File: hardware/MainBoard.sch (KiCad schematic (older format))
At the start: 47 parts, among them J10 B2_HDR_LEFT, J11 B2_HDR_RIGHT, J9 POWER, Q1 2N3904, Q2 2N3904, Q3 2N3904, U1 ATtiny85, U2 TL074, U3 78L05, U4 79L05

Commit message: [JNTUB-HW] JNTUB Hardware Revision 0.2
* Add resistor to drain C12 (PWM filter cap)
* Add optional parallel resistor to PWM filter
  * selectable by jumper
  * increases the cutoff frequency to audio range
* Add resistor between 5V and MCU RESET to allow for ISP
* Move a few resistors to Board 1
* Add ISP programming headers!
* Change all resistors and diodes to standing
* Shorten pin headers that connect Boards 1 and 2
* Ditch ground pour on Board 1 in favor of direct traces
* Move CV 1 and CV 2 jacks down a bit
* Slightly adjust LED positions
* Adjust front panel to match moved components
* Tweak design of front panel
* Fix up some 3D models
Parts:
- removed R17: 330k, SDIY:R_Axial_DIN0204_L3.6mm_D1.6mm_P5.08mm_Horizontal, symbol Device:R
- removed R21: R_out, SDIY:R_Axial_DIN0204_L3.6mm_D1.6mm_P5.08mm_Horizontal, symbol Device:R
- added J12: ISP, Pin_Headers:Pin_Header_Straight_2x03_Pitch2.54mm, symbol Connector:AVR-ISP-6
- added JP2: JMP_AUDIO, Pin_Headers:Pin_Header_Straight_1x02_Pitch2.54mm, symbol Device:Jumper_NO_Small
- added R26: 10k, Resistors_THT:R_Axial_DIN0207_L6.3mm_D2.5mm_P2.54mm_Vertical, symbol Device:R
- added R27: R_filb, Resistors_THT:R_Axial_DIN0207_L6.3mm_D2.5mm_P2.54mm_Vertical, symbol Device:R
- added R28: 100k, Resistors_THT:R_Axial_DIN0207_L6.3mm_D2.5mm_P2.54mm_Vertical, symbol Device:R
- C12: value C_filt -> C_fil
- D1, D3: footprint SDIY:D_DO-35_SOD27_P6.85mm_Horizontal -> Diodes_THT:D_DO-35_SOD27_P2.54mm_Vertical_AnodeUp
- D2, D4, D5: footprint SDIY:D_DO-35_SOD27_P6.85mm_Horizontal -> Diodes_THT:D_DO-35_SOD27_P2.54mm_Vertical_KathodeUp
- J10, J11: footprint Pin_Headers:Pin_Header_Straight_1x09_Pitch2.54mm -> Pin_Headers:Pin_Header_Straight_1x07_Pitch2.54mm; symbol Connector:Conn_01x09_Female -> Connector:Conn_01x07_Female
- JP1: value JMP_GATE_OUT -> JMP_UNIPOLAR
- R10, R11, R12, R13, R14, R16, R18, R19, R2, R20, R23, R24, R25, R4, R5, R6, R8: footprint SDIY:R_Axial_DIN0204_L3.6mm_D1.6mm_P5.08mm_Horizontal -> Resistors_THT:R_Axial_DIN0207_L6.3mm_D2.5mm_P2.54mm_Vertical
- R22: value R_filt -> R_fila; footprint SDIY:R_Axial_DIN0204_L3.6mm_D1.6mm_P5.08mm_Horizontal -> Resistors_THT:R_Axial_DIN0207_L6.3mm_D2.5mm_P2.54mm_Vertical
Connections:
- net +5V: now also R14.1, R19.1, J12.2 (VCC), R26.1; no longer R14.2, R19.2, U1.1 (~RESET~/PB5)
- net -12V: now also U4.2 (VI); no longer U4.3 (VO)
- net -5V: now also U4.3 (VO); no longer U4.2 (VI)
- net CLK_TRG: now also J11.6 (Pin_6); no longer J11.8 (Pin_8)
- net GNDREF: now also R11.1, R5.1, J12.6 (GND), R28.2; no longer J10.3 (Pin_3), J10.4 (Pin_4), J10.5 (Pin_5), J11.5 (Pin_5), J11.6 (Pin_6), R11.2, R5.2
- net MCU_ADC1: now also D1.2 (A), D2.1 (K), R2.2, R4.2, J12.3 (SCK); no longer D3.2 (A), D4.1 (K), R10.2, R8.2
- net MCU_ADC2: now also D3.2 (A), D4.1 (K), R10.2, R8.2; no longer D1.2 (A), D2.1 (K), R2.2, R4.2
- net MCU_ADC3: now also J10.6 (Pin_6); no longer J10.8 (Pin_8)
- net MCU_PB0: now also R14.2, J12.4 (MOSI); no longer R14.1
- net MCU_PWM: now also J12.1 (MISO), JP2.2, R28.1
- net OUT: now also JP1.2, R23.2, R25.2, U2.14
- net P1_AVG: now also J11.7 (Pin_7), U2.10 (+); no longer J10.9 (Pin_9), U2.5 (+)
- net P2_AVG: now also J10.7 (Pin_7), U2.5 (+); no longer J11.9 (Pin_9), U2.10 (+)
- net at R10.1, R12.1: now also U2.7; no longer U2.8
- net at Q3.3 (C): now also R19.2; no longer R19.1
- net at C12.1, R22.2, U2.12 (+): now also R27.2
- net IN_LED+ renamed CLK_LED
- net CLK_LED: now also J11.5 (Pin_5); no longer J11.7 (Pin_7)
- removed net OUT_LED+: J10.7 (Pin_7), R23.2, U2.2 (-)
- net OUT_LED- renamed LED_NEG
- net LED_NEG: now also J10.4 (Pin_4); no longer J10.6 (Pin_6)
- new net: R5.2, R6.1, U2.9 (-)
- new net: R4.1, R6.2, U2.8
- new net: R11.2, R12.2, U2.6 (-)
- new net: JP2.1, R27.1
- new net LED_POS: J10.5 (Pin_5), R23.1, U2.2 (-)
- new net MCU_RESET: J12.5 (~RST), R26.2, U1.1 (~RESET~/PB5)
- no-connect marks 0 -> 1
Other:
- note added: "330k"
- note added: "NOTES:\n\n- R_led: Will depend on the color & desired brightness. I use 5.6k for my red LEDs.\n\n- R_fila/R_filb/C_filt: Set for desired PWM filter frequencies.\n I use: R_fila = 68k R_filb = 8.2k C_filt = 2.2n\n With these values, the cutoff frequencies are:\n 1 kHz (JMP_AUDIO not set)\n 9.9 kHz (JMP_AUDIO set)\n\n- 10k resistors throughout can be replaced with anything 10k-100k.\n\n- Regular sw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"
- note added: "PWM filter"
- note added: "R17 (on Board 1)"
- note removed: "NOTES:\n\n- R_out: Use 1k for 1/4W resistors. Use 2k for 1/8W resistors.\n\n- R_led: Will depend on the color & desired brightness. I use 5.6k for my red LEDs.\n\n- R_filt/C_filt: Set for desired PWM filter freq*.\n For ATtiny85’s max 250kHz PWM, 5kHz cutoff serves well, giving:\n R_filt=47k C_filt=680p\n\n- 10k resistors in PARAM 1 and PARAM 2 can be replaced with anything 10k-100k.\n\n- Schottk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"
- moved on the sheet: C10, C12, D5, JP1, Q1, Q2, Q3, R13, R14, R16, R18, R19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

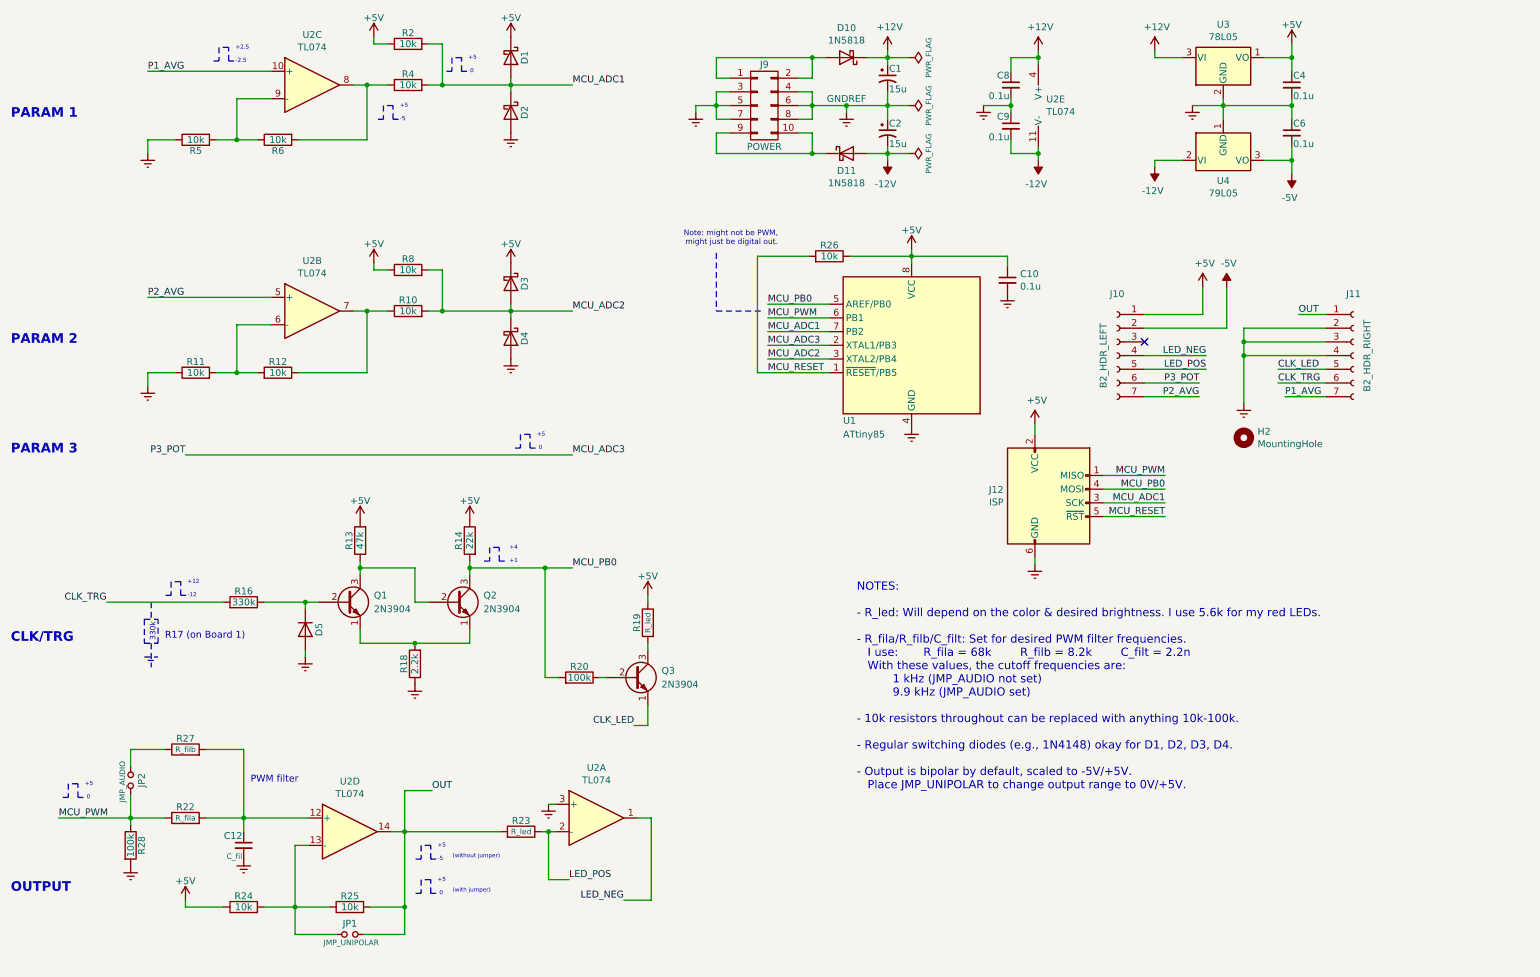
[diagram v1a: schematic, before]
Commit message: [JNTUB-HW] Modify resistor values in schematic
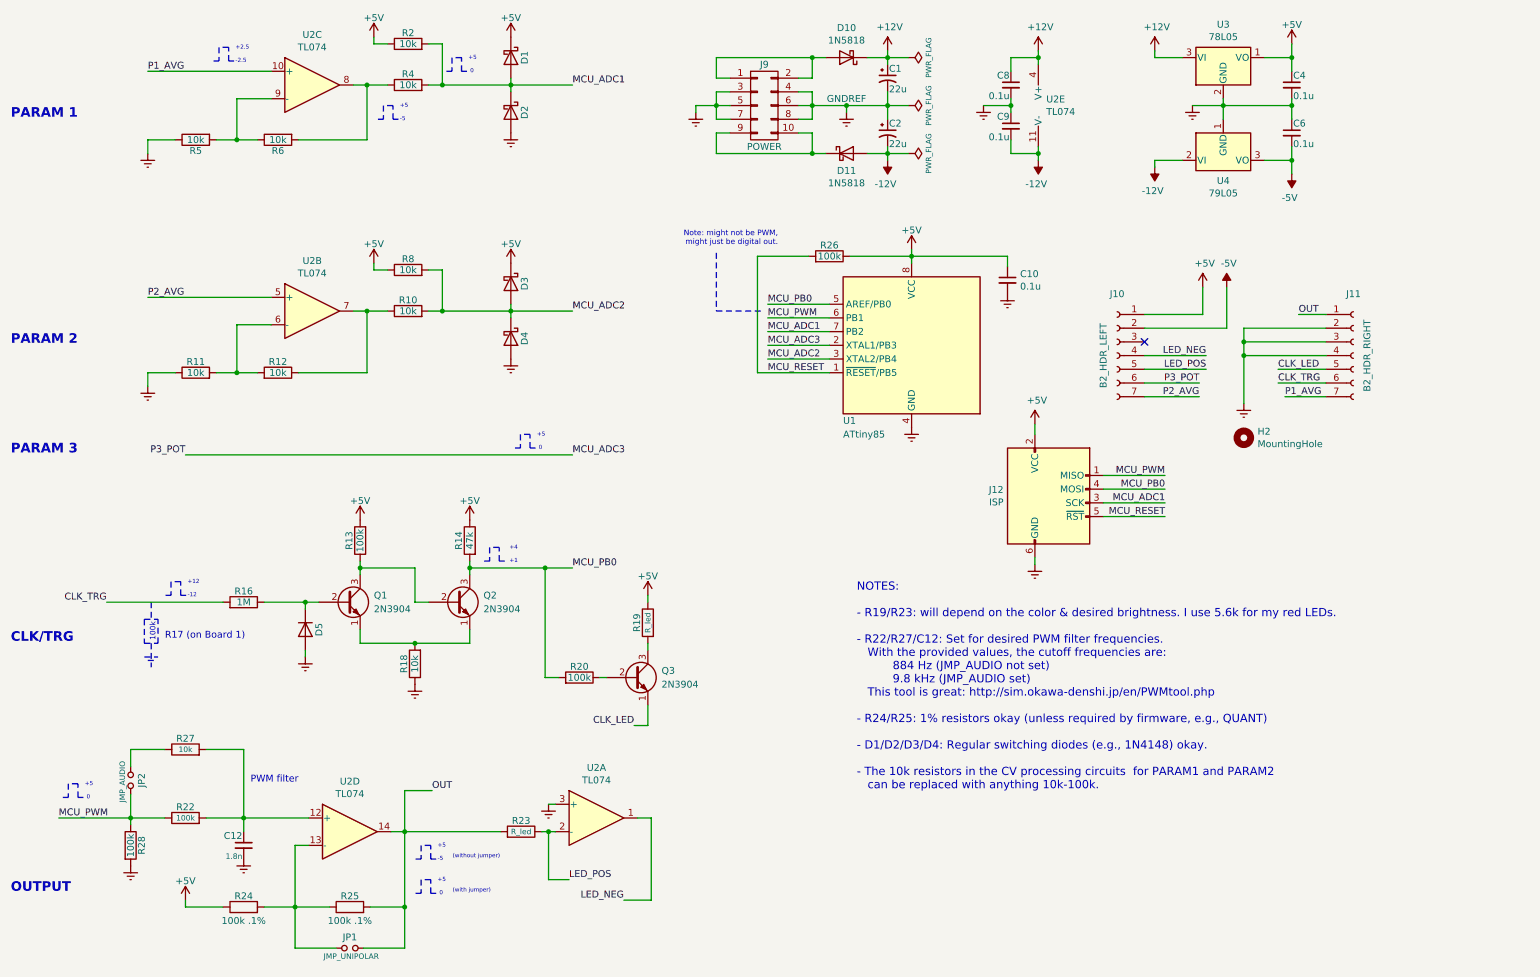
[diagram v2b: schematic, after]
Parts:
- C1, C2: value 15u -> 22u
- C12: value C_fil -> 1.8n
- R13: value 47k -> 100k
- R14: value 22k -> 47k
- R16: value 330k -> 1M
- R18: value 2.2k -> 10k
- R22: value R_fila -> 100k
- R24, R25: value 10k -> 100k .1%
- R26: value 10k -> 100k
- R27: value R_filb -> 10k
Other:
- note added: "100k"
- note added: "NOTES:\n\n- R19/R23: will depend on the color & desired brightness. I use 5.6k for my red LEDs.\n\n- R22/R27/C12: Set for desired PWM filter frequencies.\n With the provided values, the cutoff frequencies are:\n 884 Hz (JMP_AUDIO not set)\n 9.8 kHz (JMP_AUDIO set)\n This tool is great: http://sim.okawa-denshi.jp/en/PWMtool.php\n\n- R24/R25: 1% resistors okay (unless required by firmware, e.g., QU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"
- note removed: "330k"
- note removed: "NOTES:\n\n- R_led: Will depend on the color & desired brightness. I use 5.6k for my red LEDs.\n\n- R_fila/R_filb/C_filt: Set for desired PWM filter frequencies.\n I use: R_fila = 68k R_filb = 8.2k C_filt = 2.2n\n With these values, the cutoff frequencies are:\n 1 kHz (JMP_AUDIO not set)\n 9.9 kHz (JMP_AUDIO set)\n\n- 10k resistors throughout can be replaced with anything 10k-100k.\n\n- Regular sw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"
- moved on the sheet: JP1
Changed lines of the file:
@@
 P 2500 5025
 F 0 "R16" V 2580 5025 50  0000 C CNN
-F 1 "330k" V 2500 5025 50  0000 C CNN
+F 1 "1M" V 2500 5025 50  0000 C CNN
 F 2 "Resistors_THT:R_Axial_DIN0207_L6.3mm_D2.5mm_P2.54mm_Vertical" V 2430 5025 50  0001 C CNN
 F 3 "" H 2500 5025 50  0001 C CNN
@@
 P 3350 4575
 F 0 "R13" V 3430 4575 50  0000 C CNN
-F 1 "47k" V 3350 4575 50  0000 C CNN
+F 1 "100k" V 3350 4575 50  0000 C CNN
 F 2 "Resistors_THT:R_Axial_DIN0207_L6.3mm_D2.5mm_P2.54mm_Vertical" V 3280 4575 50  0001 C CNN
 F 3 "" H 3350 4575 50  0001 C CNN
@@
 P 3275 7250
 F 0 "R25" V 3355 7250 50  0000 C CNN
-F 1 "10k" V 3275 7250 50  0000 C CNN
+F 1 "100k .1%" V 3175 7250 50  0000 C CNN
 F 2 "Resistors_THT:R_Axial_DIN0207_L6.3mm_D2.5mm_P2.54mm_Vertical" V 3205 7250 50  0001 C CNN
 F 3 "" H 3275 7250 50  0001 C CNN
@@
 P 2500 7250
 F 0 "R24" V 2580 7250 50  0000 C CNN
-F 1 "10k" V 2500 7250 50  0000 C CNN
+F 1 "100k .1%" V 2400 7250 50  0000 C CNN
 F 2 "Resistors_THT:R_Axial_DIN0207_L6.3mm_D2.5mm_P2.54mm_Vertical" V 2430 7250 50  0001 C CNN
 F 3 "" H 2500 7250 50  0001 C CNN
@@
 Connection ~ 2875 7250
 Wire Wire Line
-	2875 7450 3175 7450
+	2875 7550 3175 7550
 $Comp
 L Device:Jumper_NO_Small JP1
 U 1 1 5FEB5E16
-P 3275 7450
-F 0 "JP1" H 3275 7530 50  0000 C CNN
-F 1 "JMP_UNIPOLAR" H 3285 7390 40  0000 C CNN
-F 2 "Pin_Headers:Pin_Header_Straight_1x02_Pitch2.54mm" H 3275 7450 50  0001 C CNN
-F 3 "" H 3275 7450 50  0001 C CNN
-	1    3275 7450
-	1    0    0    -1
-$EndComp
-Wire Wire Line
-	3675 7450 3375 7450
+P 3275 7550
+F 0 "JP1" H 3275 7630 50  0000 C CNN
+F 1 "JMP_UNIPOLAR" H 3285 7490 40  0000 C CNN
+F 2 "Pin_Headers:Pin_Header_Straight_1x02_Pitch2.54mm" H 3275 7550 50  0001 C CNN
+F 3 "" H 3275 7550 50  0001 C CNN
+	1    3275 7550
+	1    0    0    -1
+$EndComp
+Wire Wire Line
+	3675 7550 3375 7550
 Connection ~ 3675 7250
 $Comp
@@
 P 2500 6800
 F 0 "C12" H 2510 6870 50  0000 L CNN
-F 1 "C_fil" H 2510 6720 40  0000 L CNN
+F 1 "1.8n" H 2510 6720 40  0000 L CNN
 F 2 "Capacitors_THT:C_Disc_D4.3mm_W1.9mm_P5.00mm" H 2500 6800 50  0001 C CNN
 F 3 "" H 2500 6800 50  0001 C CNN
@@
 P 2075 6600
 F 0 "R22" V 2155 6600 50  0000 C CNN
-F 1 "R_fila" V 2075 6600 40  0000 C CNN
+F 1 "100k" V 2075 6600 40  0000 C CNN
 F 2 "Resistors_THT:R_Axial_DIN0207_L6.3mm_D2.5mm_P2.54mm_Vertical" V 2005 6600 50  0001 C CNN
 F 3 "" H 2075 6600 50  0001 C CNN
@@
 	4700 4775 4700 5575
 Wire Wire Line
-	2875 7250 2875 7450
+	2875 7250 2875 7550
 Wire Wire Line
 	2875 7250 3125 7250
 Wire Wire Line
-	3675 7250 3675 7450
+	3675 7250 3675 7550
 Wire Wire Line
 	2500 6600 2975 6600
@@
 OUTPUT
 Text Notes 6975 6400 0    60   ~ 0
-NOTES:\n\n- R_led: Will depend on the color & desired brightness. I use 5.6k for my red LEDs.\n\n- R_fila/R_filb/C_filt: Set for desired PWM filter frequencies.\n   I use:       R_fila = 68k        R_filb = 8.2k        C_filt = 2.2n\n   With these values, the cutoff frequencies are:\n          1 kHz (JMP_AUDIO not set)\n          9.9 kHz (JMP_AUDIO set)\n\n- 10k resistors throughout can be replaced with anything 10k-100k.\n\n- Regular switching diodes (e.g., 1N4148) okay for D1, D2, D3, D4.\n\n- Output is bipolar by default, scaled to -5V/+5V.\n   Place JMP_UNIPOLAR to change output range to 0V/+5V.
+NOTES:\n\n- R19/R23: will depend on the color & desired brightness. I use 5.6k for my red LEDs.\n\n- R22/R27/C12: Set for desired PWM filter frequencies.\n   With the provided values, the cutoff frequencies are:\n          884 Hz (JMP_AUDIO not set)\n          9.8 kHz (JMP_AUDIO set)\n   This tool is great: http://sim.okawa-denshi.jp/en/PWMtool.php\n\n- R24/R25: 1% resistors okay (unless required by firmware, e.g., QUANT)\n\n- D1/D2/D3/D4: Regular switching diodes (e.g., 1N4148) okay.\n\n- The 10k resistors in the CV processing circuits  for PARAM1 and PARAM2\n   can be replaced with anything 10k-100k.
 $Comp
 L power:+12V #PWR0112
@@
 P 7200 1600
 F 0 "C2" H 7210 1670 50  0000 L CNN
-F 1 "15u" H 7210 1520 50  0000 L CNN
+F 1 "22u" H 7210 1520 50  0000 L CNN
 F 2 "Capacitors_THT:CP_Radial_D6.3mm_P2.50mm" H 7200 1600 50  0001 C CNN
 F 3 "" H 7200 1600 50  0001 C CNN
@@
 P 7200 1200
 F 0 "C1" H 7210 1270 50  0000 L CNN
-F 1 "15u" H 7210 1120 50  0000 L CNN
+F 1 "22u" H 7210 1120 50  0000 L CNN
 F 2 "Capacitors_THT:CP_Radial_D6.3mm_P2.50mm" H 7200 1200 50  0001 C CNN
 F 3 "" H 7200 1200 50  0001 C CNN
@@
 P 6775 2500
 F 0 "R26" V 6855 2500 50  0000 C CNN
-F 1 "10k" V 6775 2500 50  0000 C CNN
+F 1 "100k" V 6775 2500 50  0000 C CNN
 F 2 "Resistors_THT:R_Axial_DIN0207_L6.3mm_D2.5mm_P2.54mm_Vertical" V 6705 2500 50  0001 C CNN
 F 3 "" H 6775 2500 50  0001 C CNN
@@
 P 2075 6100
 F 0 "R27" V 2155 6100 50  0000 C CNN
-F 1 "R_filb" V 2075 6100 40  0000 C CNN
+F 1 "10k" V 2075 6100 40  0000 C CNN
 F 2 "Resistors_THT:R_Axial_DIN0207_L6.3mm_D2.5mm_P2.54mm_Vertical" V 2005 6100 50  0001 C CNN
 F 3 "" H 2075 6100 50  0001 C CNN
@@
 P 4150 4575
 F 0 "R14" V 4230 4575 50  0000 C CNN
-F 1 "22k" V 4150 4575 50  0000 C CNN
+F 1 "47k" V 4150 4575 50  0000 C CNN
 F 2 "Resistors_THT:R_Axial_DIN0207_L6.3mm_D2.5mm_P2.54mm_Vertical" V 4080 4575 50  0001 C CNN
 F 3 "" H 4150 4575 50  0001 C CNN
@@
 R17 (on Board 1)
 Text Notes 1860 5310 1    40   ~ 0
-330k
+100k
 $Comp
 L Device:R R18
@@
 P 3750 5475
 F 0 "R18" V 3830 5475 50  0000 C CNN
-F 1 "2.2k" V 3750 5475 50  0000 C CNN
+F 1 "10k" V 3750 5475 50  0000 C CNN
 F 2 "Resistors_THT:R_Axial_DIN0207_L6.3mm_D2.5mm_P2.54mm_Vertical" V 3680 5475 50  0001 C CNN
 F 3 "" H 3750 5475 50  0001 C CNN
